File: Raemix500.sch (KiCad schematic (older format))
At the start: 0 parts

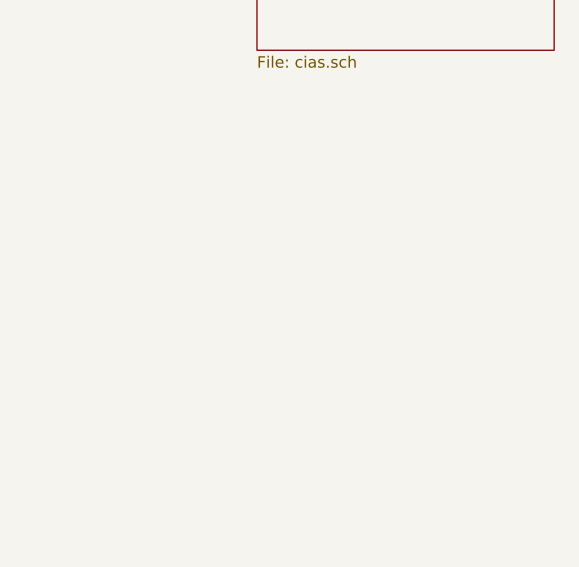
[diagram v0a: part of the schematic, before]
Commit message: Add floppy stuff, not yet complete
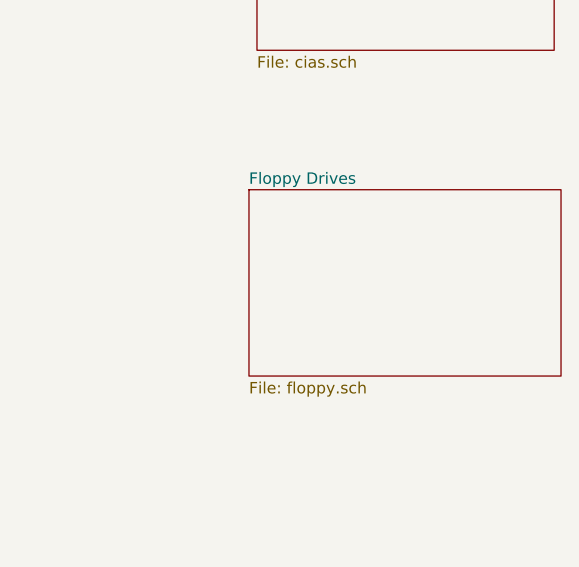
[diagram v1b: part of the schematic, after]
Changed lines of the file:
@@
 $Descr A4 11693 8268
 encoding utf-8
-Sheet 1 6
+Sheet 1 7
 Title "Rämixx500"
-Date "2019-04-16"
+Date "2019-04-17"
 Rev "1git"
 Comp "SukkoPera"
@@
 F1 "cias.sch" 50
 $EndSheet
+$Sheet
+S 4065 2780 1365 815
+U 6072A453
+F0 "Floppy Drives" 50
+F1 "floppy.sch" 50
+$EndSheet
 $EndSCHEMATC

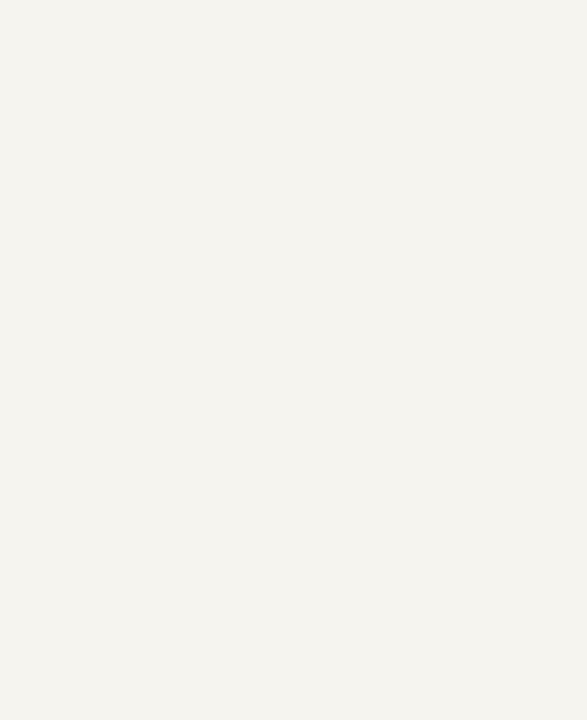
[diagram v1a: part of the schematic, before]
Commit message: Add terminators and ROM, fix bus interconnections
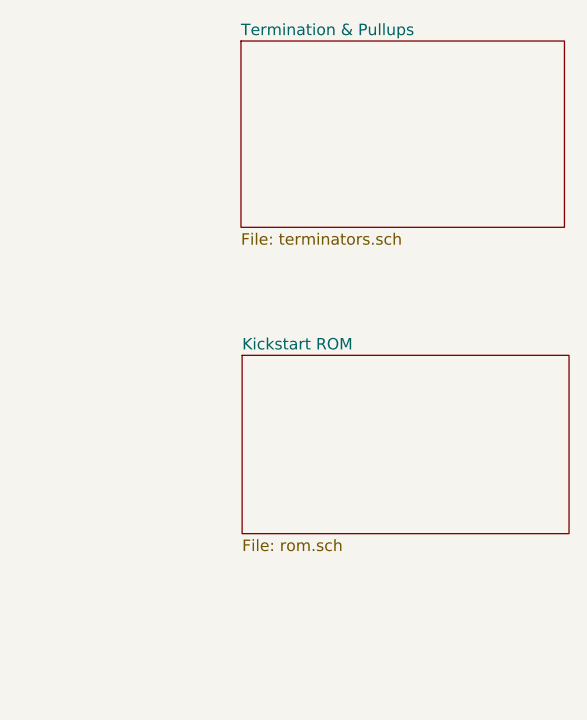
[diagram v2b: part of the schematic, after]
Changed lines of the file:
@@
 $Descr A4 11693 8268
 encoding utf-8
-Sheet 1 7
+Sheet 1 9
 Title "Rämixx500"
 Date "2019-04-17"
@@
 F1 "floppy.sch" 50
 $EndSheet
+$Sheet
+S 6905 1400 1415 815
+U 5D6D5EBE
+F0 "Termination & Pullups" 50
+F1 "terminators.sch" 50
+$EndSheet
+$Sheet
+S 6910 2775 1430 780
+U 5D86DD46
+F0 "Kickstart ROM" 50
+F1 "rom.sch" 50
+$EndSheet
 $EndSCHEMATC
